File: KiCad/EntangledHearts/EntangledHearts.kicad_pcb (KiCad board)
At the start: 2 copper layers, 147.3 x 55.9 mm, 65 parts

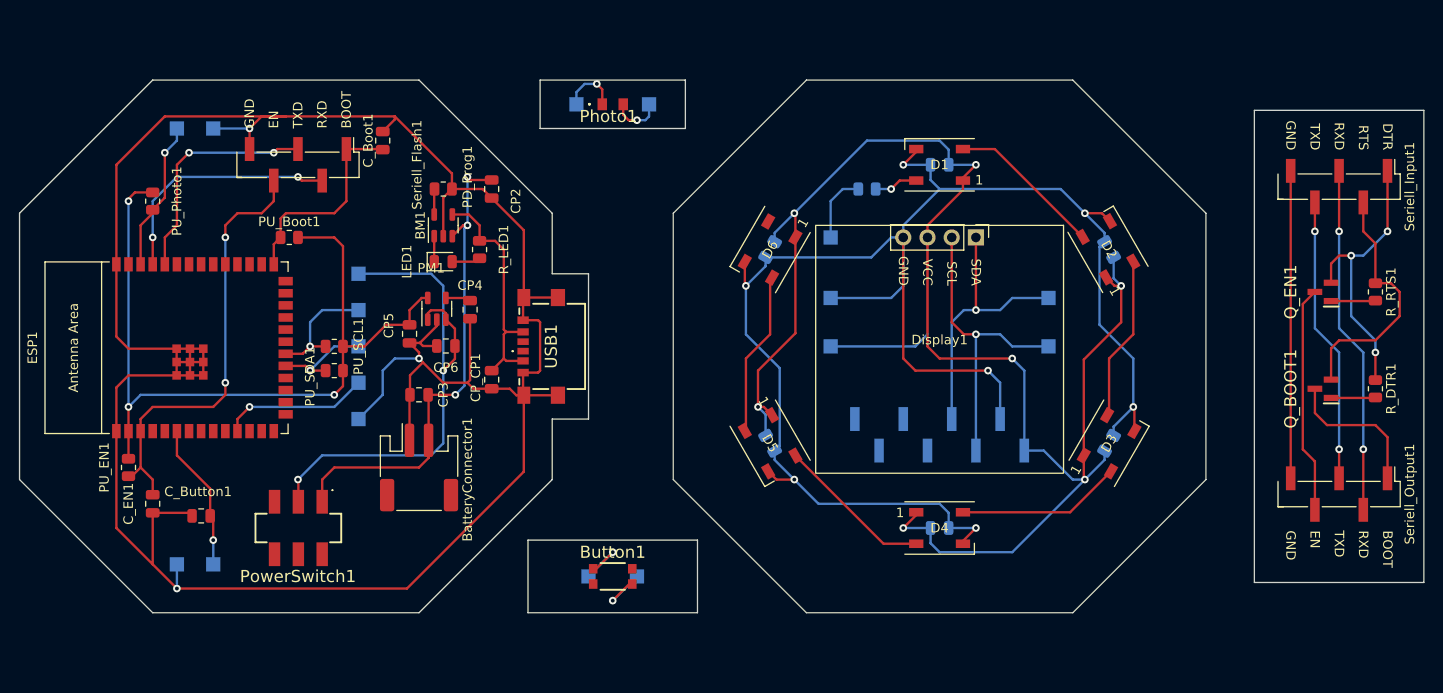
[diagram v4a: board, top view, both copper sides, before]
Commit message: ADD: mousebites added
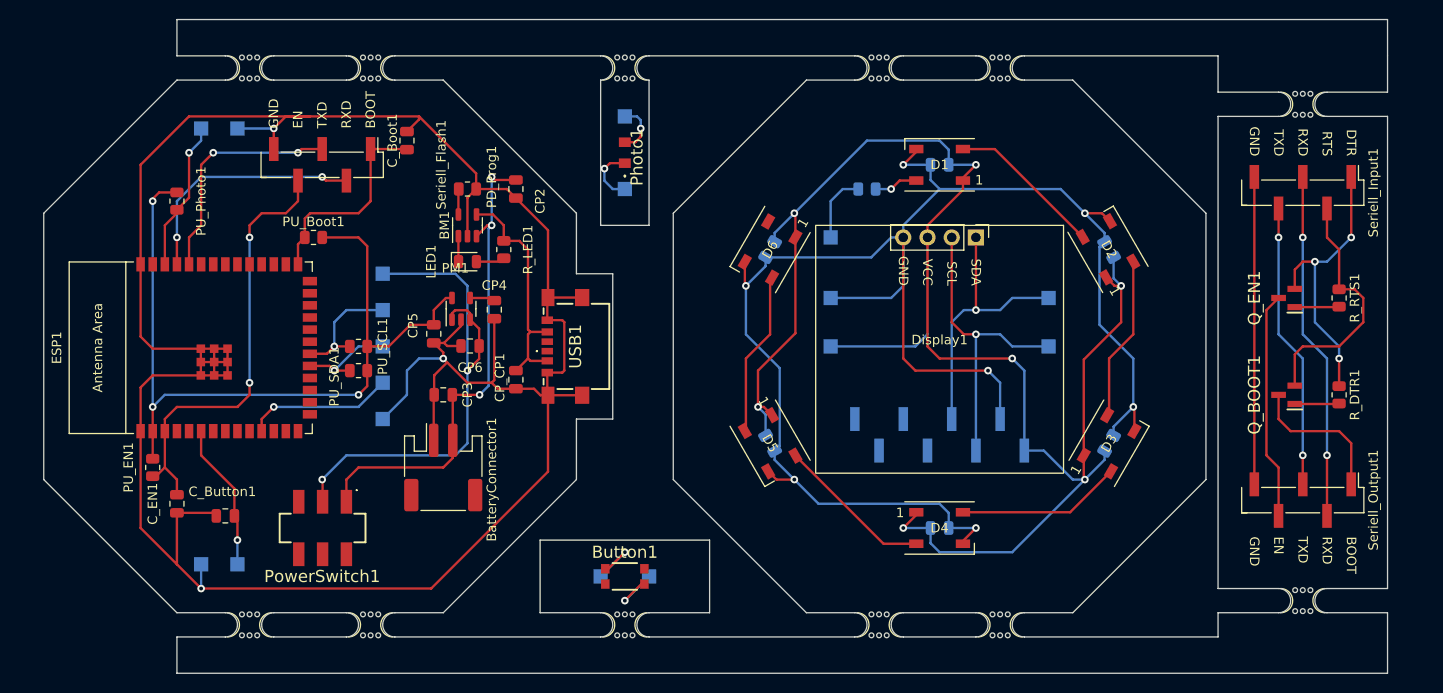
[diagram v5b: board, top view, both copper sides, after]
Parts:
- added mouse-bite-2.54mm-slot: VAL**, MouseBites:mouse-bite-2.54mm-slot, F.Cu at (108.0, 72.4)
- added mouse-bite-2.54mm-slot: VAL**, MouseBites:mouse-bite-2.54mm-slot, F.Cu at (161.3, 130.8)
- added mouse-bite-2.54mm-slot: VAL**, MouseBites:mouse-bite-2.54mm-slot, F.Cu at (205.7, 76.2)
- added mouse-bite-2.54mm-slot: VAL**, MouseBites:mouse-bite-2.54mm-slot, F.Cu at (108.0, 130.8)
- added mouse-bite-2.54mm-slot: VAL**, MouseBites:mouse-bite-2.54mm-slot, F.Cu at (134.6, 130.8)
- added mouse-bite-2.54mm-slot: VAL**, MouseBites:mouse-bite-2.54mm-slot, F.Cu at (205.7, 128.3)
- added mouse-bite-2.54mm-slot: VAL**, MouseBites:mouse-bite-2.54mm-slot, F.Cu at (134.6, 72.4)
- added mouse-bite-2.54mm-slot: VAL**, MouseBites:mouse-bite-2.54mm-slot, F.Cu at (95.2, 130.8)
- added mouse-bite-2.54mm-slot: VAL**, MouseBites:mouse-bite-2.54mm-slot, F.Cu at (174.0, 130.8)
- added mouse-bite-2.54mm-slot: VAL**, MouseBites:mouse-bite-2.54mm-slot, F.Cu at (161.3, 72.4)
- added mouse-bite-2.54mm-slot: VAL**, MouseBites:mouse-bite-2.54mm-slot, F.Cu at (174.0, 72.4)
- added mouse-bite-2.54mm-slot: VAL**, MouseBites:mouse-bite-2.54mm-slot, F.Cu at (95.2, 72.4)
- moved PhotoB2 10.2 mm to (134.6, 85.1), turned to -90 degrees
- moved Photo1 5.24 mm to (134.6, 81.3), turned to 90 degrees
- moved Q_BOOT1 3.86 mm to (204.1, 106.7)
- moved R_DTR1 3.86 mm to (209.6, 106.7)
- moved Q_EN1 3.86 mm to (204.1, 96.5)
- moved R_RTS1 3.86 mm to (209.6, 96.5)
- moved Seriell_Input1 3.86 mm to (205.7, 85.5)
- moved Seriell_Output1 3.86 mm to (205.7, 117.7)
- moved PhotoA2 2.84 mm to (134.6, 77.5), turned to 90 degrees
- moved BM1 2.54 mm to (118.1, 88.9)
- moved ButtonA1 2.54 mm to (94.0, 124.5)
- moved ButtonB1 2.54 mm to (90.2, 124.5)
- moved CP5 2.54 mm to (114.6, 100.3)
- moved CP6 2.54 mm to (118.4, 101.6)
- moved C_Boot1 2.54 mm to (111.8, 80.0)
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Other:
- board size 147.3 x 55.9 mm -> 141 x 68.6 mm

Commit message: ADD: Gerberfiles added
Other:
- board text added: "Rapid Prototyping Rev. A"
